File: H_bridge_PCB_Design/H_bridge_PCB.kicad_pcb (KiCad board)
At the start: 2 copper layers, 100 x 100 mm, 115 parts, among them IC2 L7812ABD2T-TR, IC5 ACS37800KMACTR-030B3-I2C, J1 TMS-102-21-G-S, J10 TMS-102-21-G-S, J11 TMS-102-21-G-S, J2 TMS-102-21-G-S, J3 TMS-102-21-G-S, J4 TMS-102-21-G-S, J5 TMS-102-21-G-S, J6 TMS-102-21-G-S, J7 TMS-102-21-G-S, J8 TMS-102-21-G-S, J9 TMS-102-21-G-S, P1 USB_C_Plug_USB2.0, Q1 IRLB4030PBF, Q10 IPD90N10S4L06ATMA1, Q2 IRLB4030PBF, Q3 IRLB4030PBF, Q4 IRLB4030PBF, Q5 IPD90N10S4L06ATMA1, Q6 IPD90N10S4L06ATMA1, Q7 BC817, Q8 BC817, Q9 IPD90N10S4L06ATMA1, U1 ESP32-WROOM-32, U2 IR2110S, U3 IR2110S, U4 INA228, U5 LD1086DT33TR, U6 LD1086DT50TR, U7 CH340C, U8 3544-2

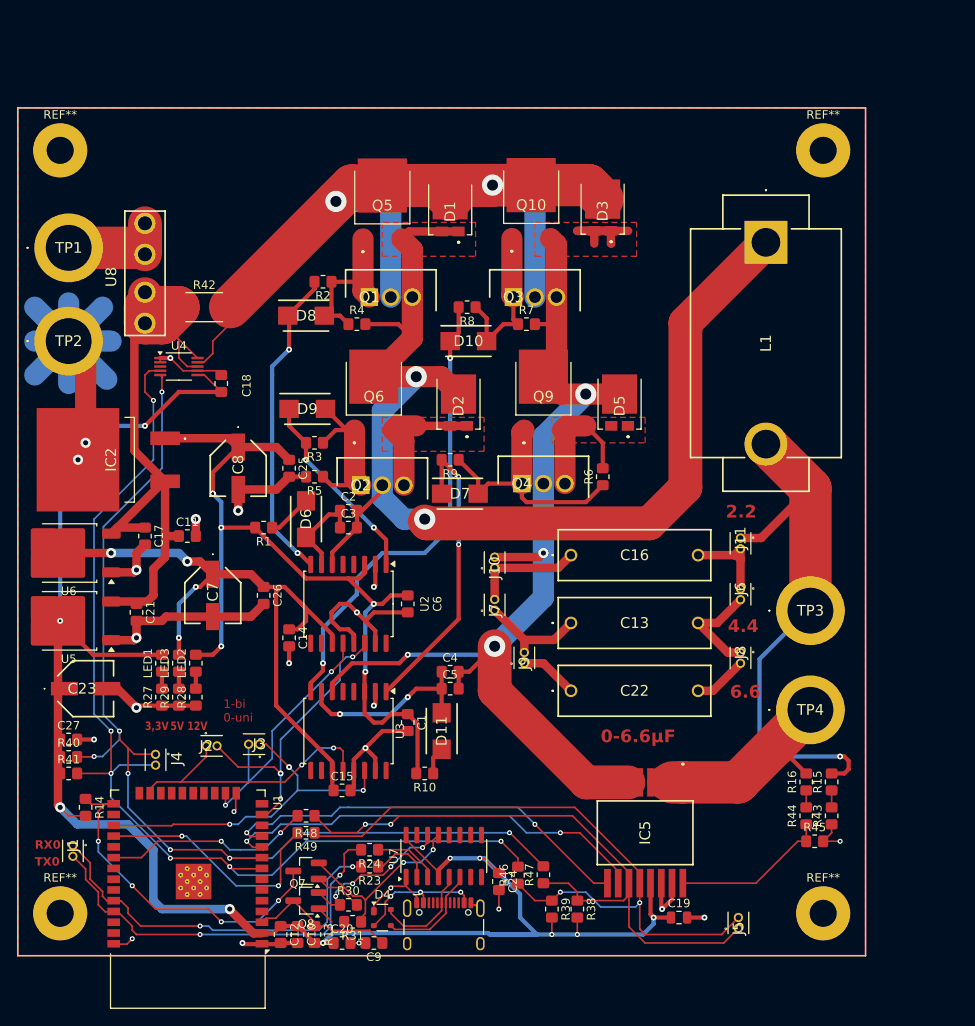
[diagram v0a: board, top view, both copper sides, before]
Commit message: Interrupt for PWM and unipolar modulation
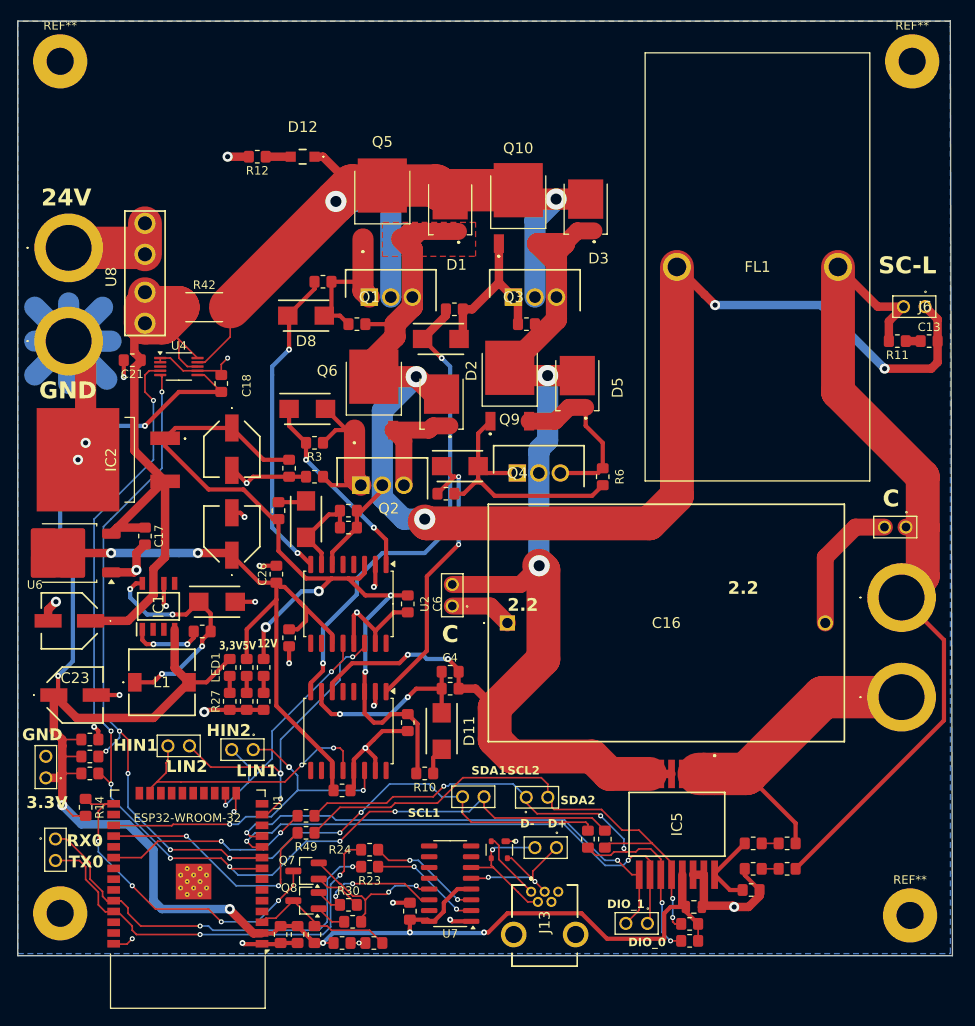
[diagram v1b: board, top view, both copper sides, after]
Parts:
- removed J10, J11, J8: TMS-102-21-G-S, SamacSys_Parts:TMS-102-YY-XX-S
- removed P1: USB_C_Plug_USB2.0, Connector_USB:USB_C_Receptacle_HCTL_HC-TYPE-C-16P-01A
- removed the REF** at (145.0, 144.5)
- removed the REF** at (145.0, 54.5)
- removed U5: LD1086DT33TR, Package_TO_SOT_SMD:TO-252-2
- added D12: HPZR-C26X, SamacSys_Parts:HPZRC26X, F.Cu at (83.6, 55.2)
- added D13: S210, SamacSys_Parts:DIOM5336X265N, F.Cu at (73.5, 107.8)
- added FL1: PHBC24N-2R0A0219V, SamacSys_Parts:PHBC24N2R0A0219V, F.Cu at (146.8, 68.2)
- added IC1: LM2671M-3.3_NOPB, SamacSys_Parts:SOIC127P600X175-8N, F.Cu at (66.6, 108.3)
- added J12: TSW-102-15-T-S, SamacSys_Parts:TSW-102-XX-YY-S, F.Cu at (124.3, 145.7)
- added J13: 1734510-1, SamacSys_Parts:17345101, F.Cu at (110.5, 141.9)
- added J14: TSW-102-15-T-S, SamacSys_Parts:TSW-102-XX-YY-S, F.Cu at (113.5, 136.8)
- added J15: TSW-102-15-T-S, SamacSys_Parts:TSW-102-XX-YY-S, F.Cu at (53.3, 128.5)
- added R11: 10, Resistor_SMD:R_0805_2012Metric_Pad1.20x1.40mm_HandSolder, F.Cu at (153.8, 77.0)
- added R12: 1, Resistor_SMD:R_0805_2012Metric_Pad1.20x1.40mm_HandSolder, F.Cu at (78.2, 55.2)
- added REF**: MountingHole_3.2mm_M3_Pad, MountingHole:MountingHole_3.2mm_M3_Pad, F.Cu at (155.2, 144.8)
- added REF**: MountingHole_3.2mm_M3_Pad, MountingHole:MountingHole_3.2mm_M3_Pad, F.Cu at (155.5, 44.0)
- C11: value 1µF -> 10 nF
- C13: value MKS4C042204C00KSSD -> 100 nF; footprint SamacSys_Parts:MKS4C042204C00KSSD -> Resistor_SMD:R_0805_2012Metric_Pad1.20x1.40mm_HandSolder
- C16: value MKS4C042204C00KSSD -> B32776E4406J000; footprint SamacSys_Parts:MKS4C042204C00KSSD -> SamacSys_Parts:B32776E4406J000
- C22: value MKS4C042204C00KSSD -> 100uF; footprint SamacSys_Parts:MKS4C042204C00KSSD -> SamacSys_Parts:EEE1AA101SP
- J1, J2, J3, J4, J5, J6, J7, J9: value TMS-102-21-G-S -> TSW-102-15-T-S; footprint SamacSys_Parts:TMS-102-YY-XX-S -> SamacSys_Parts:TSW-102-XX-YY-S
- L1: value IH15BQ5R0K -> IFDC3030EZER101M; footprint SamacSys_Parts:IH15BQ5R0K -> SamacSys_Parts:IFDC3030EZER101M
- moved L1 88.1 mm to (67.0, 117.2), turned to 0 degrees
- moved C22 59.7 mm to (56.1, 110.0), turned to 180 degrees
- moved C13 53.8 mm to (157.5, 77.0)
- moved J7 49.5 mm to (154.8, 98.9), turned to 180 degrees
- moved J6 39.8 mm to (157.0, 72.9), turned to 180 degrees
- moved J4 36.6 mm to (102.5, 130.8), turned to 0 degrees
- moved C21 29.8 mm to (63.5, 79.2), turned to 180 degrees
- moved J5 29.4 mm to (110.0, 130.8), turned to 0 degrees
- moved R39 16.3 mm to (129.2, 145.8), turned to 0 degrees
- moved D4 16.0 mm to (106.8, 137.0), turned to -90 degrees
- moved R38 13.8 mm to (129.2, 147.8), turned to 0 degrees
- moved R15 11.5 mm to (140.8, 139.2), turned to 0 degrees
- moved C11 11.4 mm to (71.8, 111.2)
- moved R43 11.2 mm to (136.8, 139.2), turned to 0 degrees
- moved R46 11.1 mm to (119.2, 135.8)
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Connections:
- C11 pad 1: SI1 -> Net-(IC1-CB)
- C11 pad 2: GND -> Net-(D13-K)
- C13 pad 2: Net-(C13-Pad2) -> Out+
- C22 pad 1: Net-(C22-Pad1) -> SI1
- C22 pad 2: Net-(C22-Pad2) -> GND
- J6 pad 1: Net-(C16-Pad2) -> Out+
- J6 pad 2: Net-(C13-Pad2) -> Cout+
- J7 pad 1: Net-(C13-Pad1) -> Cout+
- J7 pad 2: Net-(C16-Pad1) -> Net-(C16-Pad2)
- J9 pad 1: Net-(C22-Pad1) -> Net-(C16-Pad1)
- J9 pad 2: Net-(C13-Pad1) -> Cout-
- L1 pad 1: Out+ -> Net-(D13-K)
- L1 pad 2: Cout+ -> +3.3V
- U1 pad 31: U0CTS -> unconnected-(U1-IO19-Pad31)
- U1 pad 36: U0RTS -> unconnected-(U1-IO22-Pad36)
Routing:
- net Out+: track 142.3 -> 180.6 mm, vias 2 -> 4
- net Cout+: track 65.7 -> 102.0 mm, vias 1 -> 0
- net SO1: track 126.1 -> 93.1 mm
- net Net-(D13-K): track 0.00 -> 28.2 mm, vias 0 -> 4
- net SDA2: track 79.1 -> 64.2 mm
- net GND: track 229.8 -> 215.7 mm, vias 23 -> 28
- net Net-(C13-Pad2): track 12.6 -> 0.00 mm
- net SI2: track 27.0 -> 39.6 mm
- net +3.3V: track 214.8 -> 226.8 mm, vias 10 -> 7
- net SCL2: track 75.6 -> 63.9 mm, vias 2 -> 5
- net Net-(C13-Pad1): track 12.8 -> 1.75 mm
- net DIO_1: track 49.4 -> 59.6 mm
- net DIO_0: track 51.2 -> 60.6 mm
- net Net-(IC5-VINP): track 18.6 -> 9.22 mm
- net Net-(IC1-CB): track 0.00 -> 8.59 mm, vias 0 -> 2
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- removed copper zone on F.Cu, net Cout-
- removed copper zone on F.Cu, net GND
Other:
- board size 100 x 100 mm -> 110.2 x 110.2 mm
- board text added: "24V"
- board text added: "3.3V"
- board text added: "C"
- board text added: "D+"
- board text added: "D-"
- board text added: "DIO_0"
- board text added: "DIO_1"
- board text added: "GND"
- board text added: "HIN1"
- board text added: "HIN2"
- board text added: "LIN1"
- board text added: "LIN2"
- board text added: "SC-L"
- board text added: "SCL1"
- board text added: "SCL2"
- board text added: "SDA1"
- board text added: "SDA2"
- board text removed: "0-6.6µF"
- board text removed: "1-bi 0-uni"
- board text removed: "4.4"
- board text removed: "6.6"
